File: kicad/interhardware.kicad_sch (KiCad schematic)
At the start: 66 parts, among them J1 RJ11, J2 RJ11, J4 USB_C_Receptacle_USB2.0_14P, Q1 MMBTA42, Q2 MMBTA92, Q3 MMBTA42, Q4 MMBTA06, Q5 MMBTA06, SW1 SW_Omron_B3FS, U1 SI3019-F-FM, U2 SI3050-E1-FM, U3 ESP32-C3-WROOM-02, U4 TPS62162DSG

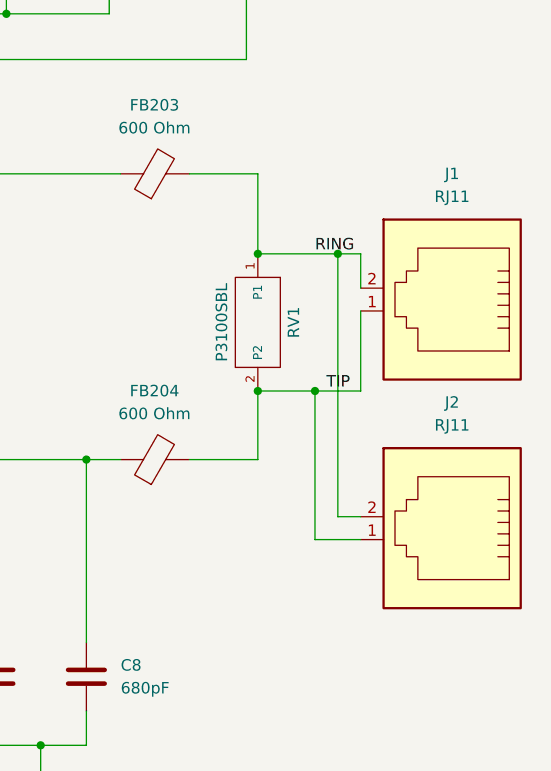
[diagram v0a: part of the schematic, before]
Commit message: trocando os RJ11
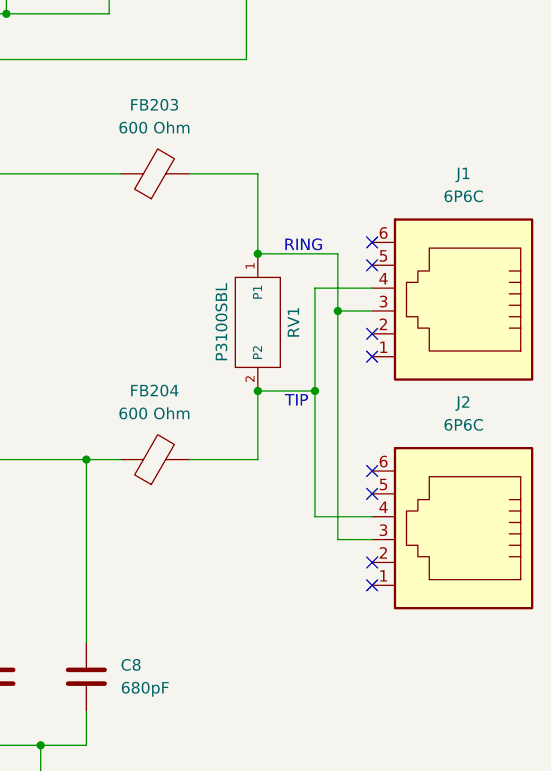
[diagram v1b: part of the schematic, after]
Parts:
- removed J1, J2: RJ11, Connector_RJ:RJ12_Amphenol_54601-x06_Horizontal, symbol Connector:RJ11
- added J1, J2: 6P6C, Connector_RJ:RJ12_Amphenol_54601-x06_Horizontal, symbol Connector:6P6C
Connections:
- net RING: no longer names the net of FB203.2, RV1.1 (P1)
- net RING: now also J1.3, J2.3
- net TIP: no longer names the net of FB204.2, RV1.2 (P2)
- net TIP: now also J1.4, J2.4
- no-connect marks 1 -> 9
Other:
- note added: "RING"
- note added: "TIP"

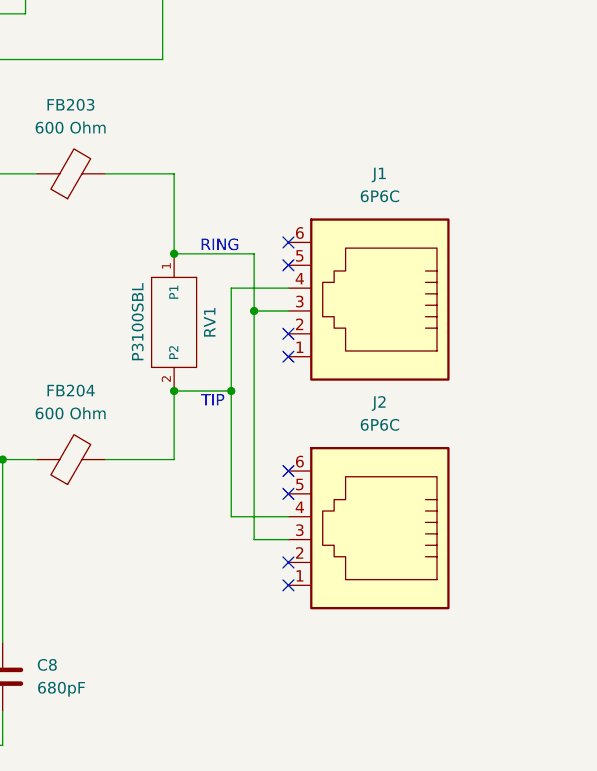
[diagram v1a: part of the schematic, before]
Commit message: rj11 existente moderno duplo
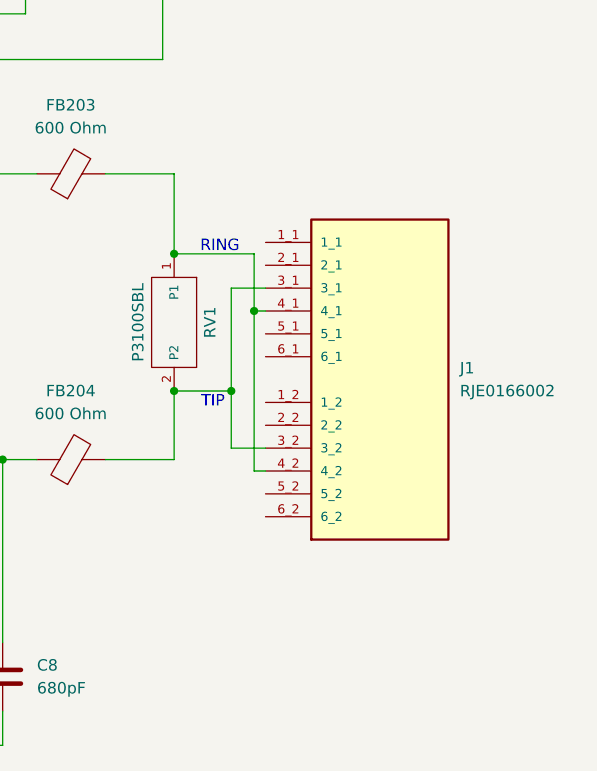
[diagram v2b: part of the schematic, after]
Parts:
- removed J1, J2: 6P6C, Connector_RJ:RJ12_Amphenol_54601-x06_Horizontal, symbol Connector:6P6C
- added J1: RJE0166002, RJE0166002:AMPHENOL_RJE0166002, symbol interbridge_telephony:RJE0166002
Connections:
- net at FB203.2, RV1.1 (P1): now also J1.4_1, J1.4_2
- net at FB204.2, RV1.2 (P2): now also J1.3_1, J1.3_2
- no-connect marks 9 -> 1

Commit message: edit
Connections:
- no-connect marks 1 -> 9
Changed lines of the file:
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@@
 		(at 96.52 149.86)
+	)
+	(no_connect
+		(at 387.35 207.01)
+	)
+	(no_connect
+		(at 387.35 189.23)
+	)
+	(no_connect
+		(at 387.35 191.77)
+	)
+	(no_connect
+		(at 387.35 199.39)
+	)
+	(no_connect
+		(at 387.35 181.61)
+	)
+	(no_connect
+		(at 387.35 179.07)
+	)
+	(no_connect
+		(at 387.35 196.85)
+	)
+	(no_connect
+		(at 387.35 209.55)
 	)
 	(wire

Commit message: finalize schematic components for PCB transfer
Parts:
- D1: MPN VERIFY -> DF04S; Manufacturer VERIFY -> TBD; Package VERIFY -> SDIP-4L bridge rectifier
- J1: MF Amphenol ICC (Commercial Products) -> (none); MP RJE0166002 -> (none); MPN (none) -> RJE0166002; Manufacturer (none) -> Amphenol Communications Solutions; Package None -> Dual 6P6C right-angle THT
- J4: value USB_C_Receptacle_USB2.0_14P -> USB4105-GF-A-060; MPN VERIFY -> USB4105-GF-A-060; Manufacturer VERIFY -> GCT; Package VERIFY -> USB Type-C, 16 contacts, top-mount horizontal; Series (none) -> USB4105
- RV1: Package DO-214AA (SMB) -> DO-214AA / SMB
- SW1: value SW_Omron_B3FS -> B3U-1000P; MPN VERIFY -> B3U-1000P; Manufacturer VERIFY -> Omron; Package VERIFY -> SMD tactile switch
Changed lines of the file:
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@@
 			)
 		)
-		(property "Description" "DF04S bridge rectifier; manufacturer and exact ordering code require verification"
+		(property "Description" "SMD bridge rectifier, 400 V class"
 			(at 321.31 186.69 0)
 			(hide yes)
@@
 			)
 		)
-		(property "Manufacturer" "VERIFY"
+		(property "Manufacturer" "TBD"
 			(at 0 0 0)
 			(hide yes)
@@
 			)
 		)
-		(property "MPN" "VERIFY"
+		(property "MPN" "DF04S"
 			(at 0 0 0)
 			(hide yes)
@@
 			)
 		)
-		(property "Package" "VERIFY"
+		(property "Package" "SDIP-4L bridge rectifier"
 			(at 0 0 0)
 			(hide yes)
@@
 			)
 		)
-		(property "Description" "Bidirectional SIDACtor surge protector, 275 V, DO-214AA"
+		(property "Description" "Bidirectional SIDACtor telecom surge protector, 275 V"
 			(at 377.19 187.96 0)
 			(hide yes)
@@
 			)
 		)
-		(property "Package" "DO-214AA (SMB)"
+		(property "Package" "DO-214AA / SMB"
 			(at 0 0 0)
 			(hide yes)
@@
 			)
 		)
-		(property "Value" "USB_C_Receptacle_USB2.0_14P"
+		(property "Value" "USB4105-GF-A-060"
 			(at 25.4 97.79 0)
 			(show_name no)
@@
 			)
 		)
-		(property "Description" "USB-C USB 2.0 receptacle; verify exact GCT USB4105 suffix and mechanics"
+		(property "Description" "USB Type-C USB 2.0 receptacle, 16 contacts, horizontal/top mount"
 			(at 25.4 118.11 0)
 			(hide yes)
@@
 			)
 		)
-		(property "Manufacturer" "VERIFY"
+		(property "Manufacturer" "GCT"
+			(at 0 0 0)
+			(hide yes)
+			(show_name no)
+			(do_not_autoplace no)
+			(effects
+				(font
+					(size 1.27 1.27)
+				)
+			)
+		)
+		(property "MPN" "USB4105-GF-A-060"
 			(at 0 0 0)
 			(hide yes)
@@
 			)
 		)
-		(property "MPN" "VERIFY"
+		(property "Package" "USB Type-C, 16 contacts, top-mount horizontal"
 			(at 0 0 0)
 			(hide yes)
@@
 			)
 		)
-		(property "Package" "VERIFY"
+		(property "Series" "USB4105"
 			(at 0 0 0)
 			(hide yes)
@@
 			)
 		)
-		(property "Description" "Modular Jack - Right Angle, Input Output Connectors 6P6C, Without Shield."
+		(property "Description" "Dual 6P6C modular jack, right-angle, through-hole"
 			(at 400.05 194.31 0)
 			(hide yes)
@@
 			)
 		)
-		(property "MF" "Amphenol ICC (Commercial Products)"
+		(property "Manufacturer" "Amphenol Communications Solutions"
 			(at 400.05 194.31 0)
 			(hide yes)
@@
 			)
 		)
-		(property "Package" "None"
+		(property "Package" "Dual 6P6C right-angle THT"
 			(at 400.05 194.31 0)
 			(hide yes)
@@
 			)
 		)
-		(property "MP" "RJE0166002"
+		(property "MPN" "RJE0166002"
 			(at 400.05 194.31 0)
 			(hide yes)
@@
 			)
 		)
-		(property "Value" "SW_Omron_B3FS"
+		(property "Value" "B3U-1000P"
 			(at 134.112 105.664 0)
 			(hide yes)
@@
 			)
 		)
-		(property "Description" "Normally-open tactile switch; symbol/footprint family mismatch requires verification"
+		(property "Description" "Normally-open SMD tactile switch"
 			(at 137.16 116.84 0)
 			(hide yes)
@@
 			)
 		)
-		(property "Manufacturer" "VERIFY"
+		(property "Manufacturer" "Omron"
 			(at 0 0 0)
 			(hide yes)
@@
 			)
 		)
-		(property "MPN" "VERIFY"
+		(property "MPN" "B3U-1000P"
 			(at 0 0 0)
 			(hide yes)
@@
 			)
 		)
-		(property "Package" "VERIFY"
+		(property "Package" "SMD tactile switch"
 			(at 0 0 0)
 			(hide yes)

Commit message: ajustando erros
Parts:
- J1: footprint RJE0166002:AMPHENOL_RJE0166002 -> interbridge_telephony:AMPHENOL_RJE0166002; MF (none) -> Amphenol ICC (Commercial Products); MP (none) -> RJE0166002; MPN RJE0166002 -> (none); Manufacturer Amphenol Communications Solutions -> (none); Package Dual 6P6C right-angle THT -> None
- U1: value SI3019-F-FM -> (none); MPN SI3019-F-FM -> (none); Manufacturer Skyworks Solutions -> (none); Package QFN-20 + exposed IGND pad -> (none)
- renumbered C_LED to C_LED1, R_bot to R_BO1, R_LED to R_LED1
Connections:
- net GND: now also J4.SH (SHIELD)
- net at J4.B7 (D-), R73.1: now also J4.A7 (D-)
- net at J4.A6 (D+), R74.1: now also J4.B6 (D+)
- no-connect marks 9 -> 17

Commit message: erros ERC Corrigidos
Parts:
- removed RV1: P3100SBL, Diode_SMD:D_SMB, symbol EVB_2PIN
- added RV1: P3100SBL, Diode_SMD:D_SMB, symbol Diode:Z2SMBxxx
- U2: value SI3050-E1-FM -> (none); footprint interbridge_telephony:3050-E1-FM-QFN50P400X400X80-25N -> (none); MPN SI3050-E1-FM -> (none); Manufacturer Skyworks Solutions -> (none); Package QFN-24 + exposed GND pad -> (none)
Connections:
- net at FB203.2, J1.4_1, J1.4_2: now also RV1.1 (K)
- net at FB204.2, J1.3_1, J1.3_2: now also RV1.2 (A)

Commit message: pcb completa
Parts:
- removed D1: DF04S, Diode_SMD:Diode_Bridge_OnSemi_SDIP-4L, symbol Diode_Bridge:DF04S
- removed J4: USB4105-GF-A-060, Connector_USB:USB_C_Receptacle_GCT_USB4105-xx-A_16P_TopMnt_Horizontal, symbol Connector:USB_C_Receptacle_USB2.0_14P
- added D1: MB6S, Package_TO_SOT_SMD:TO-269AA, symbol Diode_Bridge:MB6S
- added J2: USB_C_Receptacle_USB2.0_16P, Connector_USB:USB_C_Receptacle_GCT_USB4105-xx-A_16P_TopMnt_Horizontal, symbol Connector:USB_C_Receptacle_USB2.0_16P
- U2: footprint (none) -> interbridge_telephony:3050-E1-FM-QFN50P400X400X80-25N
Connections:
- net GND: now also J2.A1 (GND), J2.A12 (GND), J2.B1 (GND), J2.B12 (GND), J2.SH (SHIELD)
- net IGND: now also D1.1
- net at C31.1, FB2.1, R32.2: now also D1.4 (-)
- net at C75.1, C_LED1.1, D2.4 (VDD)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: now also J2.A4 (VBUS), J2.A9 (VBUS), J2.B4 (VBUS), J2.B9 (VBUS)
- net at R73.1: now also J2.A7 (D-), J2.B7 (D-)
- net at C10.1, C3.1, Q1.3 (C)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: now also D1.2
- net at C30.1, FB1.1, R30.2: now also D1.3 (+)
- net at FB204.2, RV1.2 (A): now also J1.4_1, J1.4_2; no longer J1.3_1, J1.3_2
- net at FB203.2, RV1.1 (K): now also J1.3_1, J1.3_2; no longer J1.4_1, J1.4_2
- net at R74.1: now also J2.A6 (D+), J2.B6 (D+)
- net at R71.1: now also J2.A5 (CC1)
- net at R72.1: now also J2.B5 (CC2)
- no-connect marks 17 -> 22
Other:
- moved on the sheet: RV1

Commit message: ajuste do D1
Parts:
- removed D1: MB6S, Package_TO_SOT_SMD:TO-269AA, symbol Diode_Bridge:MB6S
- added D1: MDB6S, Package_SO:TSSOP-4_4.4x5mm_P4mm, symbol Diode_Bridge:MDB6S
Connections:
- net IGND: now also D1.3
- net at C31.1, FB2.1, R32.2: now also D1.2 (-)
- net at C30.1, FB1.1, R30.2: now also D1.1 (+)
- net at C10.1, C3.1, Q1.3 (C)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: now also D1.4
- no-connect marks 22 -> 19
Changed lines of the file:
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@@
 	)
 	(no_connect
-		(at 308.61 195.58)
-	)
-	(no_connect
 		(at 387.35 191.77)
 	)
@@
 	)
 	(no_connect
-		(at -102.87 116.84)
-	)
-	(no_connect
-		(at 196.85 170.18)
-	)
-	(no_connect
 		(at 184.15 107.95)
 	)
@@
 	)
 	(symbol
+		(lib_id "Diode_Bridge:MDB6S")
+		(at 321.31 186.69 270)
+		(unit 1)
+		(body_style 1)
+		(exclude_from_sim no)
+		(in_bom yes)
+		(on_board yes)
+		(in_pos_files yes)
+		(dnp no)
+		(fields_autoplaced yes)
+		(property "Reference" "D1"
+			(at 331.47 180.2698 90)
+			(show_name no)
+			(do_not_autoplace no)
+			(effects
+				(font
+					(size 1.27 1.27)
+				)
+			)
+		)
+		(property "Value" "MDB6S"
+			(at 331.47 182.8098 90)
+			(show_name no)
+			(do_not_autoplace no)
+			(effects
+				(font
+					(size 1.27 1.27)
+				)
+			)
+		)
+		(property "Footprint" "Package_SO:TSSOP-4_4.4x5mm_P4mm"
+			(at 321.31 186.69 0)
+			(hide yes)
+			(show_name no)
+			(do_not_autoplace no)
+			(effects
+				(font
+					(size 1.27 1.27)
+				)
+			)
+		)
+		(property "Datasheet" "https://www.onsemi.com/pub/Collateral/MDB8S-D.PDF"
+			(at 321.31 186.69 0)
+			(hide yes)
+			(show_name no)
+			(do_not_autoplace no)
+			(effects
+				(font
+					(size 1.27 1.27)
+				)
+			)
+		)
+		(property "Description" "Single-Phase Bridge Rectifier, 420V Vrms, 1A If, TSSOP-4"
+			(at 321.31 186.69 0)
+			(hide yes)
+			(show_name no)
+			(do_not_autoplace no)
+			(effects
+				(font
+					(size 1.27 1.27)
+				)
+			)
+		)
+		(pin "4"
+		)
+		(pin "3"
+		)
+		(pin "1"
+		)
+		(pin "2"
+		)
+		(instances
+			(project "interhardware"
+				(path "/54dcf537-a517-4a60-ba81-f3f59fcd6b9a"
+					(reference "D1")
+					(unit 1)
+				)
+			)
+		)
+	)
+	(symbol
 		(lib_id "Device:C")
 		(at 241.3 168.91 90)
@@
 					(unit 1)
 				)
-			)
-		)
-	)
-	(symbol
-		(lib_id "Diode_Bridge:MB6S")
-		(at 321.31 186.69 270)
-		(unit 1)
-		(body_style 1)
-		(exclude_from_sim no)
-		(in_bom yes)
-		(on_board yes)
-		(in_pos_files yes)
-		(dnp no)
-		(fields_autoplaced yes)
-		(property "Reference" "D1"
-			(at 330.2 180.2698 90)
-			(show_name no)
-			(do_not_autoplace no)
-			(effects
-				(font
-					(size 1.27 1.27)
-				)
-			)
-		)
-		(property "Value" "MB6S"
-			(at 330.2 182.8098 90)
-			(show_name no)
-			(do_not_autoplace no)
-			(effects
-				(font
-					(size 1.27 1.27)
-				)
-			)
-		)
-		(property "Footprint" "Package_TO_SOT_SMD:TO-269AA"
-			(at 324.485 190.5 0)
-			(hide yes)
-			(show_name no)
-			(do_not_autoplace no)
-			(effects
-				(font
-					(size 1.27 1.27)
-				)
-				(justify left)
-			)
-		)
-		(property "Datasheet" "http://www.vishay.com/docs/88573/dfs.pdf"
-			(at 321.31 186.69 0)
-			(hide yes)
-			(show_name no)
-			(do_not_autoplace no)
-			(effects
-				(font
-					(size 1.27 1.27)
-				)
-			)
-		)
-		(property "Description" "Miniature Glass Passivated Single-Phase Surface Mount Bridge Rectifiers, 700V Vrms, 1.0A If, DFS SMD package"
-			(at 321.31 186.69 0)
-			(hide yes)
-			(show_name no)
-			(do_not_autoplace no)
-			(effects
-				(font
-					(size 1.27 1.27)
-				)
-			)
-		)
-		(property "MPN" "MB4S"
-			(at 321.31 186.69 90)
-			(hide yes)
-			(show_name no)
-			(do_not_autoplace no)
-			(effects
-				(font
-					(size 1.27 1.27)
-				)
-			)
-		)
-		(property "Package" "SOIC4-W"
-			(at 321.31 186.69 90)
-			(hide yes)
-			(show_name no)
-			(do_not_autoplace no)
-			(effects
-				(font
-					(size 1.27 1.27)
-				)
-			)
-		)
-		(property "Manufacturer" "onsemi"
-			(at 321.31 186.69 90)
-			(hide yes)
-			(show_name no)
-			(do_not_autoplace no)
-			(effects
-				(font
-					(size 1.27 1.27)
-				)
-			)
-		)
-		(pin "4"
-		)
-		(pin "2"
-		)
-		(pin "3"
-		)
-		(pin "1"
-		)
-		(instances
-			(project "interhardware"
-				(path "/54dcf537-a517-4a60-ba81-f3f59fcd6b9a"
-					(reference "D1")
-					(unit 1)
-				)
